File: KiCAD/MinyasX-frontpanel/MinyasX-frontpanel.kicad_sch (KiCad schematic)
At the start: 29 parts, among them J2001 Conn_02x06_Odd_Even, J2002 Conn_01x04, SW2001 SW_Push, SW2002 SW_Push, U2001 SLG46826G(V2), U2002 PCA9515DP, U2003 JOYSTICK

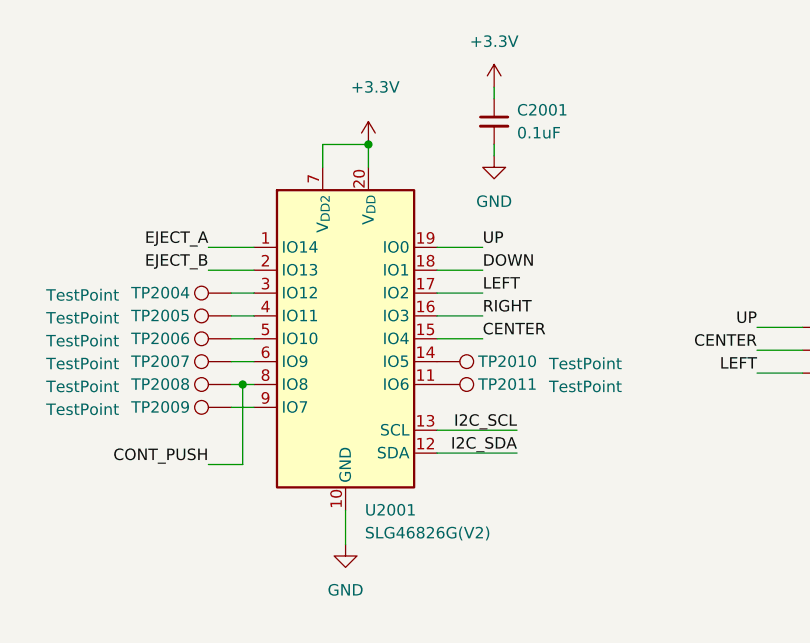
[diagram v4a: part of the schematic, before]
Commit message: 細かい基板のパッチを当てた * MODE_SELECT をGPからドライブできるように配線した * FDD電源出力コネクタを少し外に出した * GP1、GP5のI2Cを切り離せるようにした * GP5のI2C を5V系に変更 * WCH-LinkE の接続コネクタが鏡像になっていた問題を修正
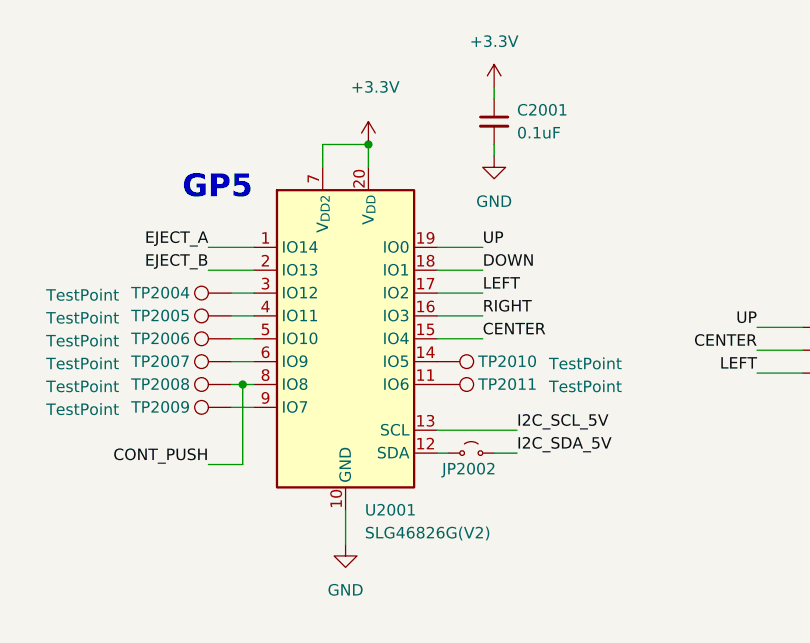
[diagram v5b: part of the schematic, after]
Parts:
- added JP2002: Jumper_2_Small_Open, Jumper:SolderJumper-2_P1.3mm_Open_RoundedPad1.0x1.5mm, symbol Jumper:Jumper_2_Small_Open
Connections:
- net I2C_SCL: no longer U2001.13 (SCL)
- net I2C_SCL_5V: now also U2001.13 (SCL)
- net I2C_SDA: no longer U2001.12 (SDA)
- net I2C_SDA_5V: now also JP2002.2 (B)
- new net: JP2002.1 (A), U2001.12 (SDA)
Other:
- note added: "GP5"
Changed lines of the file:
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@@
 	(generator_version "9.0")
 	(paper "A4")
+	(text "GP5"
+		(exclude_from_sim no)
+		(at 82.296 110.236 0)
+		(effects
+			(font
+				(size 2.54 2.54)
+				(thickness 0.508)
+				(bold yes)
+			)
+		)
+	)
 	(junction
 		(at 60.96 66.04)
@@
 	(wire
 		(pts
+			(xy 113.03 139.7) (xy 115.57 139.7)
+		)
+		(stroke
+			(width 0)
+			(type default)
+		)
+	)
+	(wire
+		(pts
 			(xy 25.4 22.86) (xy 25.4 27.94)
 		)
@@
 	(wire
 		(pts
-			(xy 106.68 139.7) (xy 115.57 139.7)
+			(xy 106.68 139.7) (xy 107.95 139.7)
 		)
 		(stroke
@@
 		)
 	)
-	(label "I2C_SCL"
-		(at 115.57 137.16 180)
+	(label "I2C_SCL_5V"
+		(at 115.57 137.16 0)
 		(effects
 			(font
 				(size 1.27 1.27)
 			)
-			(justify right bottom)
+			(justify left bottom)
 		)
 	)
@@
 		)
 	)
-	(label "I2C_SDA"
-		(at 115.57 139.7 180)
+	(label "I2C_SDA_5V"
+		(at 115.57 139.7 0)
 		(effects
 			(font
 				(size 1.27 1.27)
 			)
-			(justify right bottom)
+			(justify left bottom)
 		)
 	)
@@
 					(unit 1)
 				)
+			)
+		)
+	)
+	(symbol
+		(lib_id "Jumper:Jumper_2_Small_Open")
+		(at 110.49 139.7 0)
+		(unit 1)
+		(exclude_from_sim no)
+		(in_bom yes)
+		(on_board yes)
+		(dnp no)
+		(property "Reference" "JP2002"
+			(at 110.236 141.478 0)
+			(effects
+				(font
+					(size 1.27 1.27)
+				)
+			)
+		)
+		(property "Value" "Jumper_2_Small_Open"
+			(at 110.49 135.89 0)
+			(effects
+				(font
+					(size 1.27 1.27)
+				)
+				(hide yes)
+			)
+		)
+		(property "Footprint" "Jumper:SolderJumper-2_P1.3mm_Open_RoundedPad1.0x1.5mm"
+			(at 110.49 139.7 0)
+			(effects
+				(font
+					(size 1.27 1.27)
+				)
+				(hide yes)
+			)
+		)
+		(property "Datasheet" "~"
+			(at 110.49 139.7 0)
+			(effects
+				(font
+					(size 1.27 1.27)
+				)
+				(hide yes)
+			)
+		)
+		(property "Description" "Jumper, 2-pole, small symbol, open"
+			(at 110.49 139.7 0)
+			(effects
+				(font
+					(size 1.27 1.27)
+				)
+				(hide yes)
+			)
+		)
+		(pin "2"
+		)
+		(pin "1"
+		)
+		(instances
+			(project "MinyasX-frontpanel"
+				(path "/80e520bf-7441-4877-abbb-ba5bde50a5a4"
+					(reference "JP2002")
+					(unit 1)
+				)
